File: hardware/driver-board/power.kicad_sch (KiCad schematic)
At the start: 21 parts, among them SW2 MT-O-102-C003-N003-RS, U5 LMR51430XDDCR

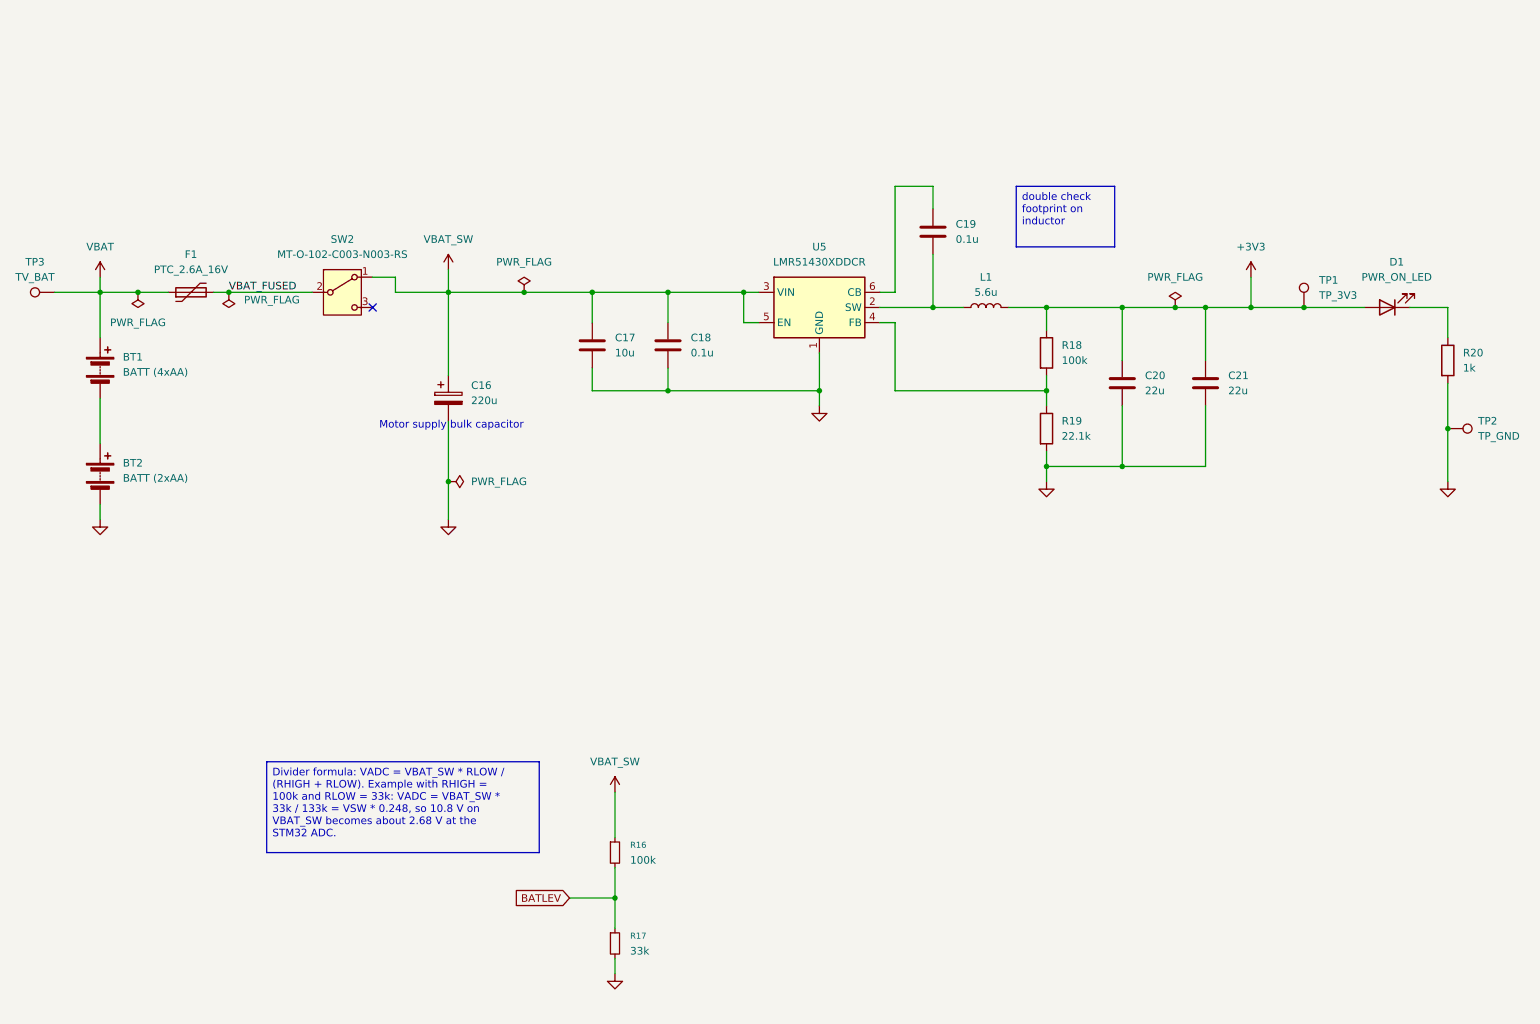
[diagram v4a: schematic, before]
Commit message: Update driver board power schematic
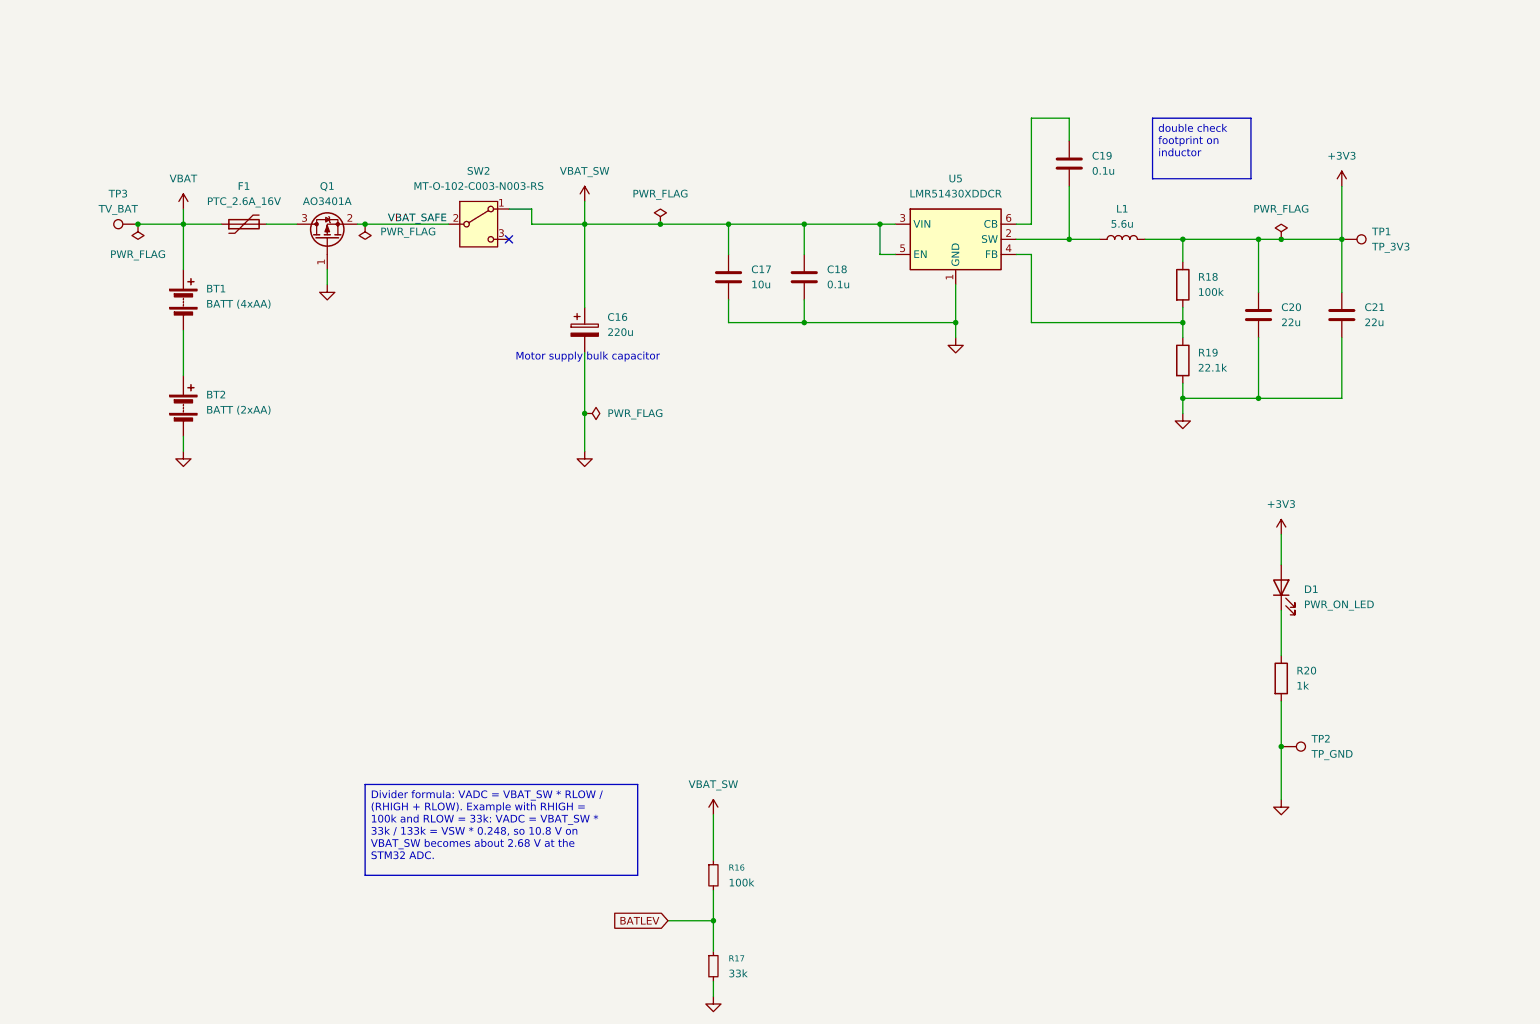
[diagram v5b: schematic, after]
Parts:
- added Q1: AO3401A, Package_TO_SOT_SMD:SOT-23, symbol Transistor_FET:AO3401A
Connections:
- net GND: now also Q1.1 (G)
- net VBAT_FUSED: no longer names the net of F1.2
- net VBAT_FUSED: now also Q1.3 (D); no longer SW2.2 (B)
- new net VBAT_SAFE: Q1.2 (S), SW2.2 (B)
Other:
- moved on the sheet: BT1, BT2, C16, C17, C18, C19, C20, C21, D1, F1, L1, R16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

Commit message: Complete Romi-compatible board placement and power switching
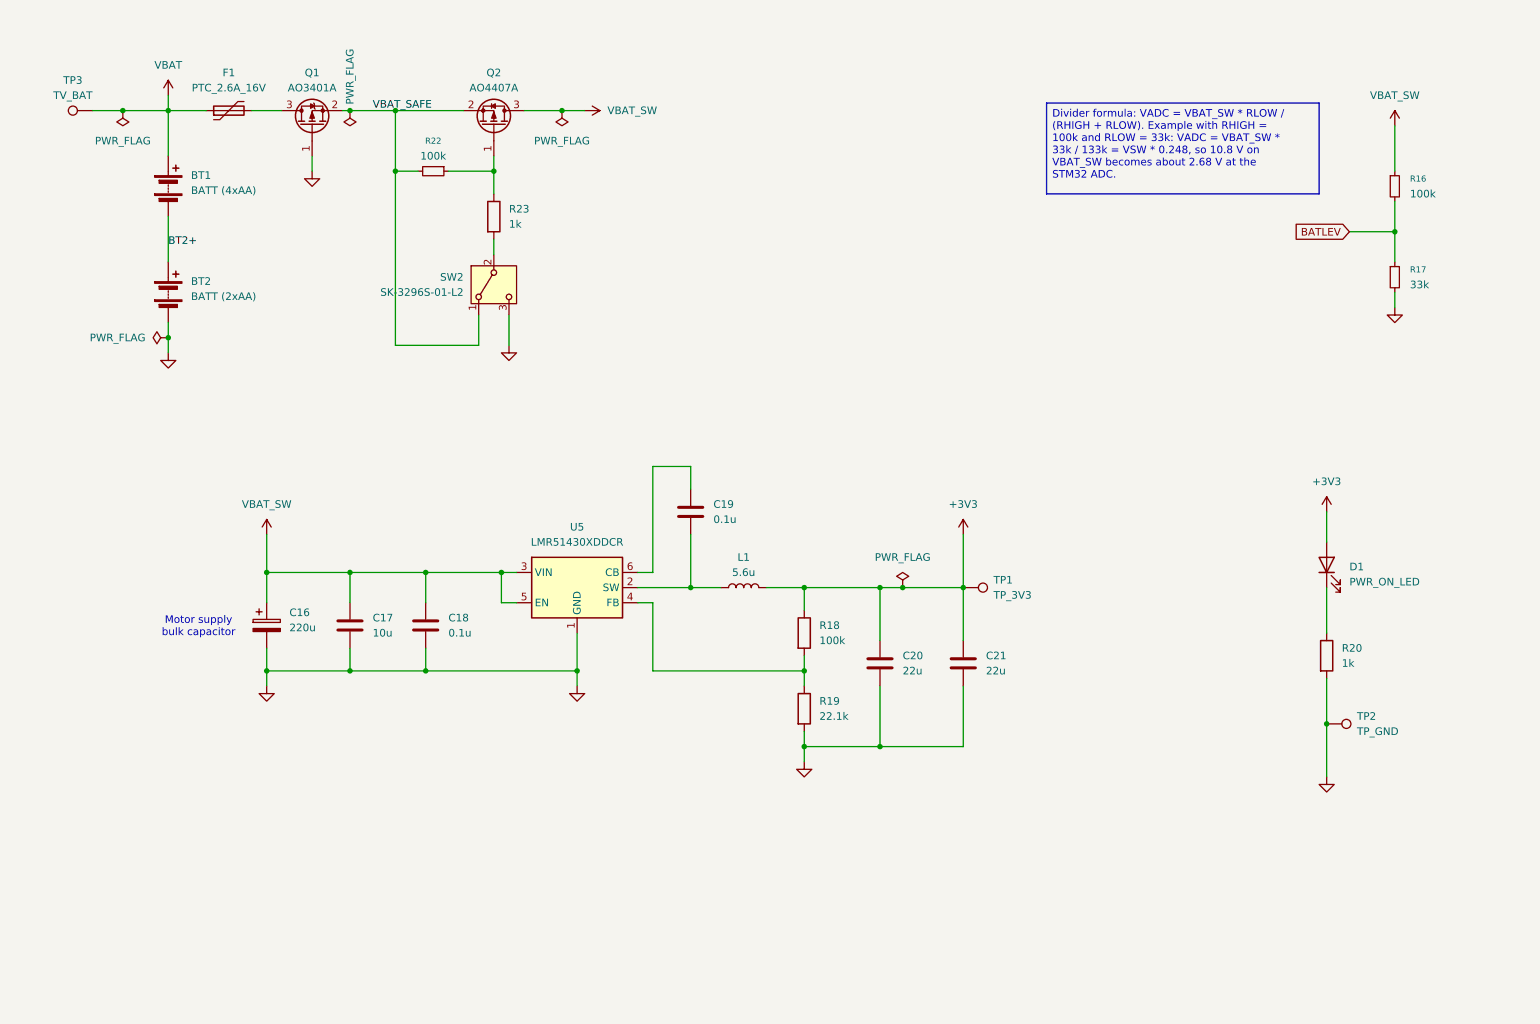
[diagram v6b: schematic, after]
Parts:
- added Q2: AO4407A, CustomParts:AO4407A_SO-8_GSD, symbol Transistor_FET:Q_PMOS_GSD
- added R22: 100k, Resistor_SMD:R_0603_1608Metric, symbol Device:R_Small
- added R23: 1k, Resistor_SMD:R_0603_1608Metric, symbol Device:R
- BT1, BT2: footprint CustomParts:Romi_Chassis_BatteryContactPair_2Slot_10_44mm_FirstPass -> CustomParts:Romi_Chassis_BatteryContactPair_2Slot_14_50mm
- Q1: JLCPCB (none) -> C15127; JLCPCB Type (none) -> Basic
- SW2: value MT-O-102-C003-N003-RS -> SK-3296S-01-L2; footprint CustomParts:SW_SPDT_Angled_YuenFung_MT-O-102-C003-N003-RS -> CustomParts:SW_SPDT_RightAngle_XKB_SK-3296S-01-L2; JLCPCB C1788495 -> C500051; JLCPCB Type Extended -> (none); MPN MT-O-102-C003-N003-RS -> (none); Manufacturer YUE FUNG -> (none)
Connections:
- net GND: now also SW2.3 (C)
- net VBAT_SAFE: now also SW2.1 (A), Q2.2 (S), R22.2; no longer SW2.2 (B)
- net VBAT_SW: now also Q2.3 (D); no longer SW2.1 (A)
- net BT2+: now reaches BT1.2 (-), BT2.1 (+)
- new net: Q2.1 (G), R22.1, R23.1
- new net: R23.2, SW2.2 (B)
- no-connect marks 1 -> 0
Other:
- moved on the sheet: BT1, BT2, C16, C17, C18, C19, C20, C21, D1, F1, L1, Q1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

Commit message: Review and harden Rev A driver board
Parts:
- added TP4: TP_BAT_SW, TestPoint:TestPoint_Pad_2.0x2.0mm, symbol PCM_4ms_Connector:TestPoint
- L1: footprint Inductor_SMD:L_Sunlord_SWPA6045S -> Inductor_SMD:L_APV_ANR8065; JLCPCB C96960 -> C96977
- TP3: value TV_BAT -> TP_BAT
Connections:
- net VBAT_SW: now also TP4.1
- net VBAT_FUSED: now reaches F1.2, Q1.3 (D)
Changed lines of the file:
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@@
 		)
 	)
+	(label "VBAT_FUSED"
+		(at 67.31 35.56 270)
+		(effects
+			(font
+				(size 1.27 1.27)
+			)
+			(justify right bottom)
+		)
+	)
 	(global_label "BATLEV"
 		(shape input)
@@
 	)
 	(symbol
+		(lib_id "PCM_4ms_Connector:TestPoint")
+		(at 116.84 35.56 0)
+		(unit 1)
+		(body_style 1)
+		(exclude_from_sim no)
+		(in_bom yes)
+		(on_board yes)
+		(in_pos_files yes)
+		(dnp no)
+		(fields_autoplaced yes)
+		(property "Reference" "TP4"
+			(at 119.38 30.9879 0)
+			(show_name no)
+			(do_not_autoplace no)
+			(effects
+				(font
+					(size 1.27 1.27)
+				)
+				(justify left)
+			)
+		)
+		(property "Value" "TP_BAT_SW"
+			(at 119.38 33.5279 0)
+			(show_name no)
+			(do_not_autoplace no)
+			(effects
+				(font
+					(size 1.27 1.27)
+				)
+				(justify left)
+			)
+		)
+		(property "Footprint" "TestPoint:TestPoint_Pad_2.0x2.0mm"
+			(at 121.92 35.56 0)
+			(hide yes)
+			(show_name no)
+			(do_not_autoplace no)
+			(effects
+				(font
+					(size 1.27 1.27)
+				)
+			)
+		)
+		(property "Datasheet" ""
+			(at 121.92 35.56 0)
+			(hide yes)
+			(show_name no)
+			(do_not_autoplace no)
+			(effects
+				(font
+					(size 1.27 1.27)
+				)
+			)
+		)
+		(property "Description" "test point"
+			(at 116.84 35.56 0)
+			(hide yes)
+			(show_name no)
+			(do_not_autoplace no)
+			(effects
+				(font
+					(size 1.27 1.27)
+				)
+			)
+		)
+		(pin "1"
+		)
+		(instances
+			(project "driver-board"
+				(path "/3304d5f8-08d9-4046-829b-96d64a4f111d/d2d3ca0b-722e-42a4-98a9-bfa302c4313a"
+					(reference "TP4")
+					(unit 1)
+				)
+			)
+		)
+	)
+	(symbol
 		(lib_id "Device:R")
 		(at 157.48 123.19 0)
@@
 			)
 		)
-		(property "Footprint" "Inductor_SMD:L_Sunlord_SWPA6045S"
+		(property "Footprint" "Inductor_SMD:L_APV_ANR8065"
 			(at 147.32 115.57 0)
 			(hide yes)
@@
 			)
 		)
-		(property "Description" "5.6uH, Isat >= 4.5-5A, Irms >= 3A"
+		(property "Description" "SWPA8065S5R6MT, 5.6uH ±20%, Isat 8.0A min, Irms 4.5A min, DCR 26mΩ max"
 			(at 147.32 115.57 0)
 			(hide yes)
@@
 			)
 		)
-		(property "JLCPCB" "C96960"
+		(property "JLCPCB" "C96977"
 			(at 147.32 115.57 90)
 			(hide yes)
@@
 			)
 		)
-		(property "Value" "TV_BAT"
+		(property "Value" "TP_BAT"
 			(at 34.798 33.02 90)
 			(show_name no)

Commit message: Refine driver board placement and capacitor footprints
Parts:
- C17: footprint Capacitor_SMD:C_1206_3216Metric -> Capacitor_SMD:C_0805_2012Metric; JLCPCB C13585 -> C15850
- C18, C19: value 0.1u -> 100n; footprint Capacitor_SMD:C_0603_1608Metric -> Capacitor_SMD:C_0402_1005Metric; JLCPCB C14663 -> C307331
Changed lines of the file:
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@@
 			)
 		)
-		(property "Value" "0.1u"
+		(property "Value" "100n"
 			(at 97.79 123.1899 0)
 			(show_name no)
@@
 			)
 		)
-		(property "Footprint" "Capacitor_SMD:C_0603_1608Metric"
+		(property "Footprint" "Capacitor_SMD:C_0402_1005Metric"
 			(at 94.9452 125.73 0)
 			(hide yes)
@@
 			)
 		)
-		(property "JLCPCB" "C14663"
+		(property "JLCPCB" "C307331"
 			(at 93.98 121.92 0)
 			(hide yes)
@@
 			)
 		)
-		(property "Footprint" "Capacitor_SMD:C_1206_3216Metric"
+		(property "Footprint" "Capacitor_SMD:C_0805_2012Metric"
 			(at 82.2452 125.73 0)
 			(hide yes)
@@
 			)
 		)
-		(property "JLCPCB" "C13585"
+		(property "JLCPCB" "C15850"
 			(at 81.28 121.92 0)
 			(hide yes)
@@
 			)
 		)
-		(property "Value" "0.1u"
+		(property "Value" "100n"
 			(at 142.24 104.1399 0)
 			(show_name no)
@@
 			)
 		)
-		(property "Footprint" "Capacitor_SMD:C_0603_1608Metric"
+		(property "Footprint" "Capacitor_SMD:C_0402_1005Metric"
 			(at 139.3952 106.68 0)
 			(hide yes)
@@
 			)
 		)
-		(property "JLCPCB" "C14663"
+		(property "JLCPCB" "C307331"
 			(at 138.43 102.87 0)
 			(hide yes)
